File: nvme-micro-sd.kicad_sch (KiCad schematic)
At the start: 30 parts, among them J6 MicroSD_1140084168, J7 Bus_M.2_1-2199230-6, M2 Mech_M2_2280_H2.5mm

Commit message: [#53804] Clean SD&NVMe sch; Change NVMe to x4; Update 3V3 power sch
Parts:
- removed D14: SP3011-06UTG, antmicro-footprints:USON-14_3.5x1.35_P0.5mm, symbol antmicroTVSDiodes:SP3011-06UTG
- added D? (x2): PUSB3F96X_PASS, antmicro-footprints:Nexperia_DFN-10_2.5x1mm_P0.5mm, symbol antmicroTVSDiodes:PUSB3F96X_PASS
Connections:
- net GND: now also D?.3 (GND), D?.3 (GND), D?.8 (GND), D?.8 (GND)
- net SDIO.CLK: now also D?.5 (CH4), D?.6 (CH4)
- net SDIO.CMD: now also D?.1 (CH1), D?.10 (CH1)
- net SDIO.D0: now also D?.4 (CH3), D?.7 (CH3)
- net SDIO.D1: now also D?.2 (CH2), D?.9 (CH2)
- net SDIO.D2: now also D?.5 (CH4), D?.6 (CH4)
- net SDIO.D3: now also D?.4 (CH3), D?.7 (CH3)
- net at J6.9 (CD1), R81.2: now also D?.1 (CH1), D?.10 (CH1)
- net NVMe.TX3_N: now reaches J7.11 (PET3_N)
- net NVMe.TX3_P: now reaches J7.13 (PET3_P)
- net NVMe.RX2_N: now reaches J7.17 (PER2_N)
- net NVMe.RX2_P: now reaches J7.19 (PER2_P)
- net NVMe.TX2_N: now reaches J7.23 (PET2_N)
- net NVMe.TX2_P: now reaches J7.25 (PET2_P)
- net NVMe.RX1_N: now reaches J7.29 (PER1_N)
- net NVMe.RX1_P: now reaches J7.31 (PER1_P)
- net NVMe.TX1_N: now reaches J7.35 (PET1_N)
- net NVMe.TX1_P: now reaches J7.37 (PET1_P)
- net NVMe.RX3_N: now reaches J7.5 (PER3_N)
- net NVMe.RX3_P: now reaches J7.7 (PER3_P)
- net 3V3_RPi renamed +3V3
- net +3V3: now also D?.2 (CH2), D?.9 (CH2)
- net GPIO3 renamed SDIO.CD
- net NVMe.RX_N renamed NVMe.RX0_N
- net NVMe.RX_P renamed NVMe.RX0_P
- net NVMe.TX_N renamed NVMe.TX0_N
- net NVMe.TX_P renamed NVMe.TX0_P
- net PCIE_CLK_nREQ renamed NVMe.~{CLK_REQ}
- net PCIE_WAKE: no longer names the net of J7.54 (~{PEWAKE}), R89.2
- net PSCIE_nRST renamed NVMe.~{RST}
- no-connect marks 17 -> 4
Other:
- note added: "Micro SD card slot"
- note added: "Note: CM4 supports only PCIe 2.0x1"
- note removed: "Micro CD card slot"
- note removed: "TODO"
- moved on the sheet: C42, C43, C44, C45, C46, C47, C48, C49, C50, C51, C52, C53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

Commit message: [#53804] Visual cleanup for m.2/SD sch
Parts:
- removed C49, C50, C51: C_100n_0603, antmicro-footprints:C_0603_1608Metric, symbol antmicroCapacitors0603:C_100n_0603
- removed C52, C53, C54: C_1n_0603, antmicro-footprints:C_0603_1608Metric, symbol antmicroCapacitors0603:C_1n_0603
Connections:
- net +3V3: now also D?.5 (CH4), D?.6 (CH4); no longer D?.2 (CH2), D?.9 (CH2)
- net GND: now also SP9.1
- net SDIO.CD: now also D?.5 (CH4), D?.6 (CH4)
- net SDIO.CLK: now also D?.1 (CH1), D?.10 (CH1); no longer D?.5 (CH4), D?.6 (CH4)
- net SDIO.CMD: now also D?.4 (CH3), D?.7 (CH3); no longer D?.1 (CH1), D?.10 (CH1)
- net SDIO.D0: now also D?.2 (CH2), D?.9 (CH2); no longer D?.4 (CH3), D?.7 (CH3)
- net SDIO.D1: now also D?.4 (CH3), D?.7 (CH3); no longer D?.2 (CH2), D?.9 (CH2)
- net SDIO.D2: now also D?.1 (CH1), D?.10 (CH1); no longer D?.5 (CH4), D?.6 (CH4)
- net SDIO.D3: now also D?.2 (CH2), D?.9 (CH2); no longer D?.4 (CH3), D?.7 (CH3)
- net at J6.9 (CD1), R81.2: no longer D?.1 (CH1), D?.10 (CH1)
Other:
- note added: "Note: Place close to pins 12,14,16,18"
- note added: "Note: Place close to pins 2,4"
- note added: "Note: Place close to pins 70,72,74"
- note removed: "Capacitor cluster for pins 12,14,16,18"
- note removed: "Capacitor cluster for pins 2,4"
- note removed: "Capacitor cluster for pins 70,72,74"
- moved on the sheet: C42, C43, C44, C45, C46, C47, C48, D15, D?, J6, J7, M2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

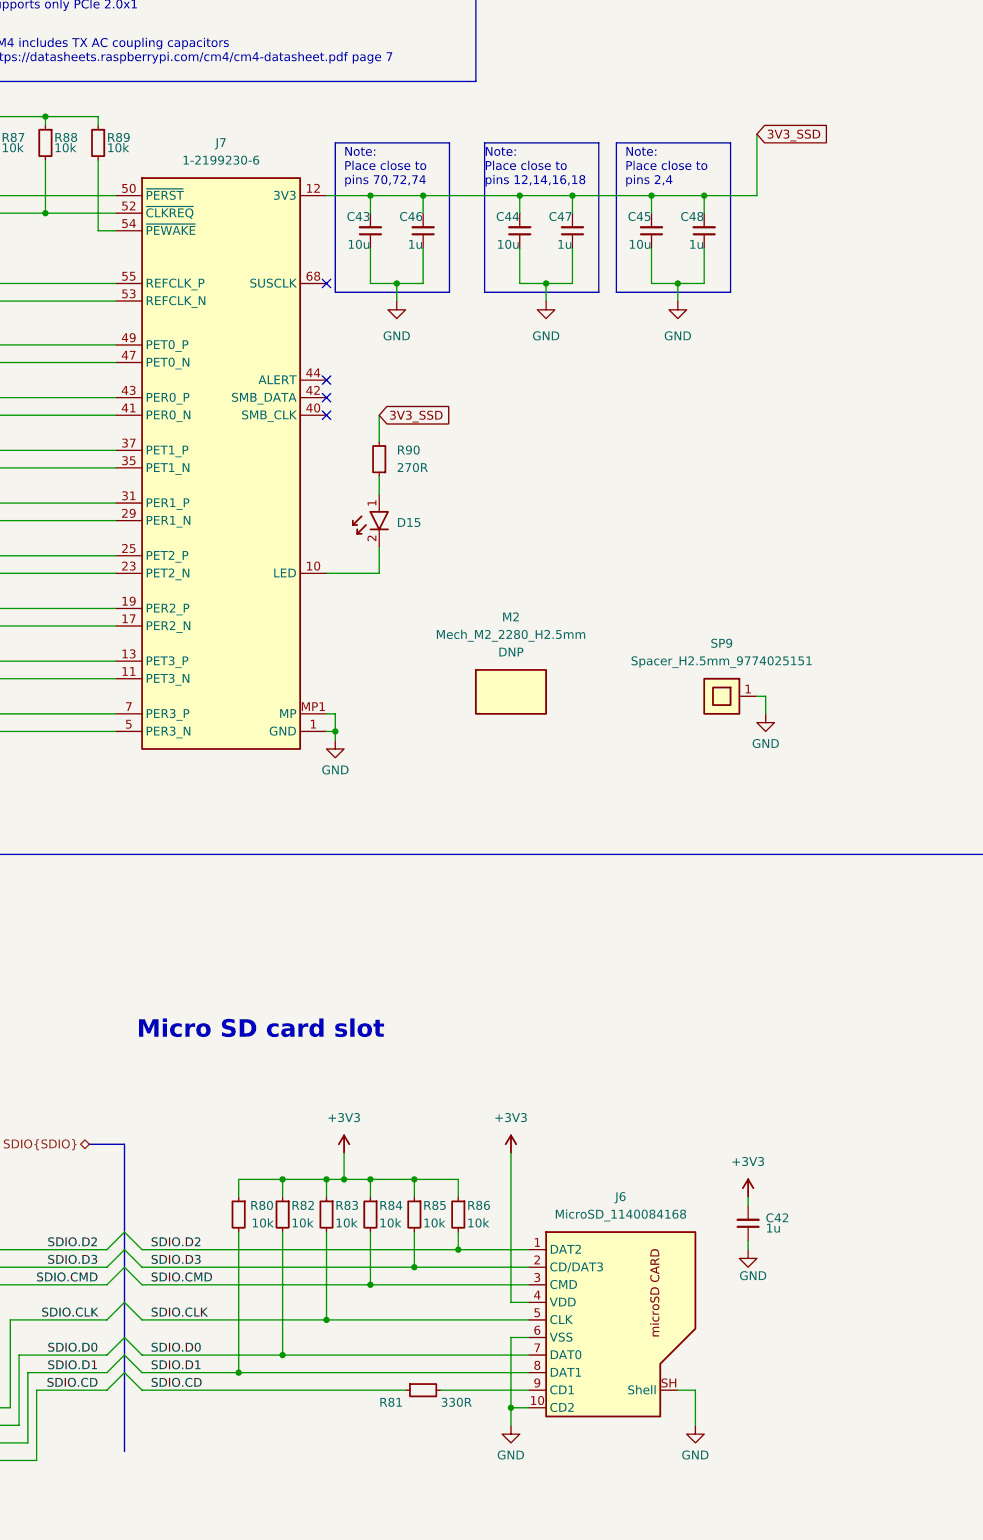
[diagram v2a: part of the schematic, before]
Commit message: [#54617] Apply changes pointed in review, related to nvme-micro-sd
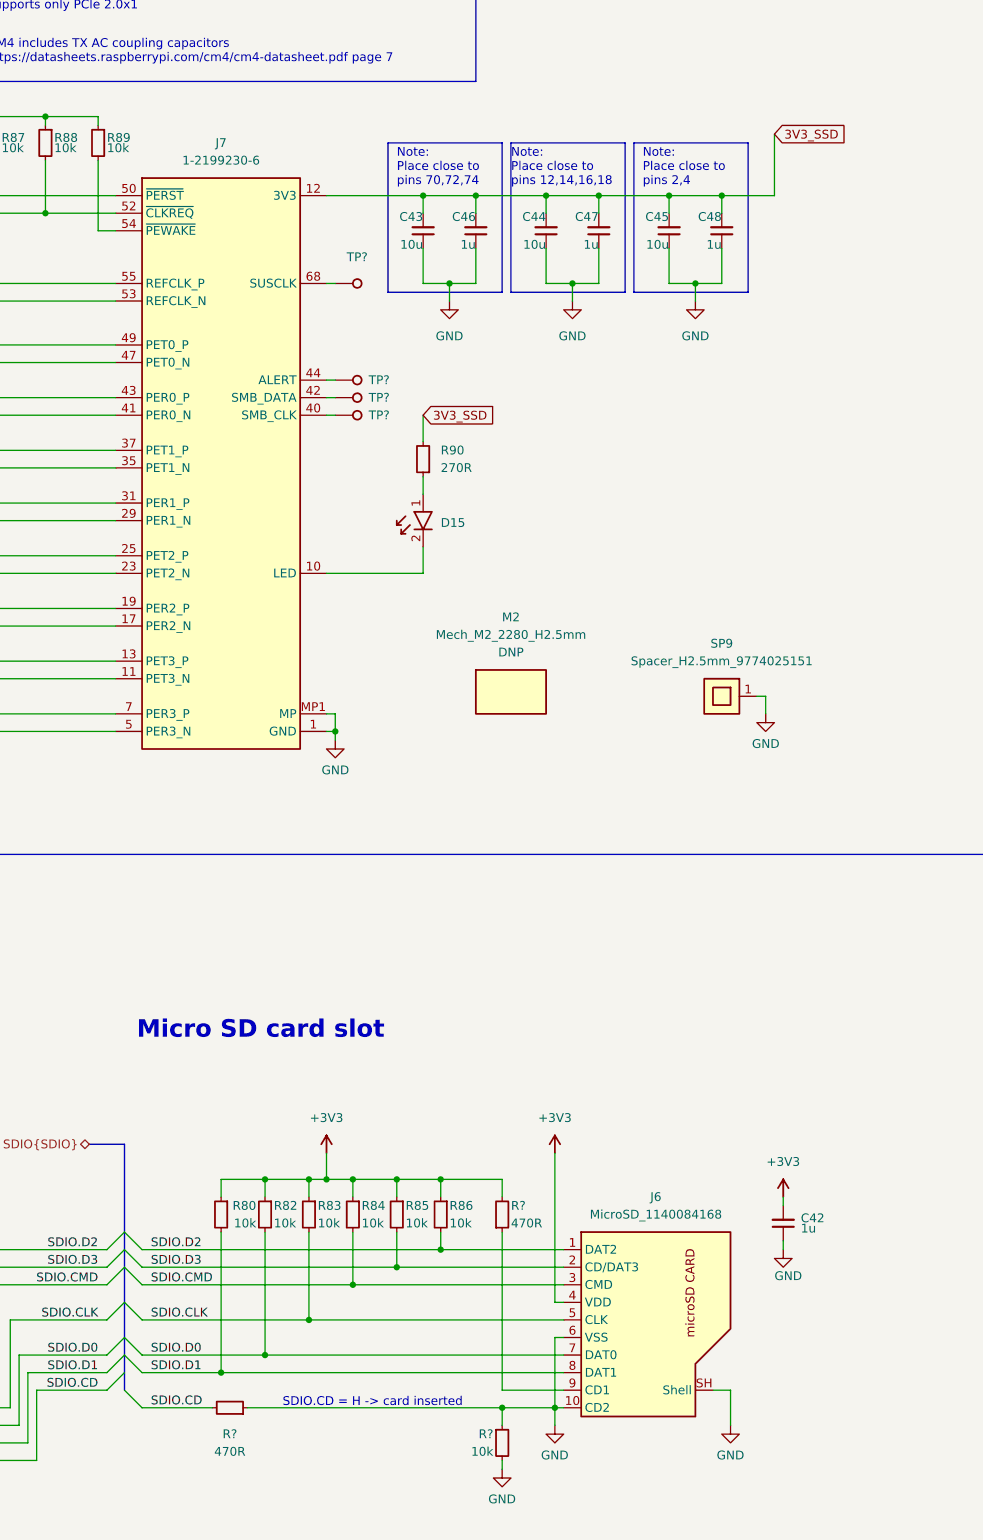
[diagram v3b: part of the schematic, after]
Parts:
- removed R81: R_330R_0402, antmicro-footprints:R_0402_1005Metric, symbol antmicroResistors0402:R_330R_0402
- added R? (x2): R_470R_0402, antmicro-footprints:R_0402_1005Metric, symbol antmicroResistors0402:R_470R_0402
- added R?: R_10k_0402, antmicro-footprints:R_0402_1005Metric, symbol antmicroResistors0402:R_10k_0402
- added TP? (x4): TP_0.75mm_SMD, antmicro-footprints:TP_SMD_0.75mm, symbol antmicroTestPoints:TP_0.75mm_SMD
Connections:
- net +3V3: now also R?.2
- net GND: now also R?.1, R?.1, R?.2
- net SDIO.CD: now also R?.2
- net at J6.9 (CD1): now also R?.1
- net at J7.40 (SMB_CLK): now also TP?.1
- net at J7.42 (SMB_DATA): now also TP?.1
- net at J7.44 (ALERT): now also TP?.1
- net at J7.68 (SUSCLK): now also TP?.1
- no-connect marks 4 -> 0
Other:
- note added: "SDIO.CD = H -> card inserted"
- moved on the sheet: C42, C43, C44, C45, C46, C47, C48, D15, J6, R80, R82, R83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

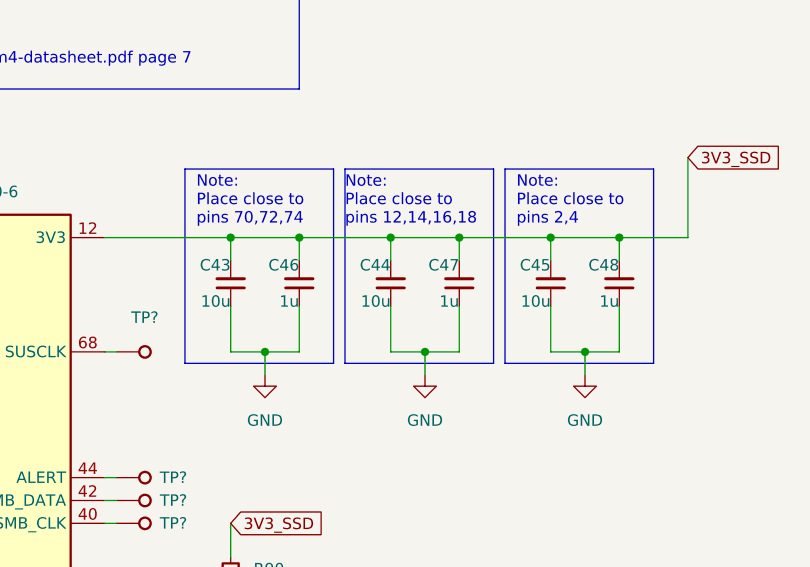
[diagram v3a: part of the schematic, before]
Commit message: [#54617] Reduce capacitors diversity
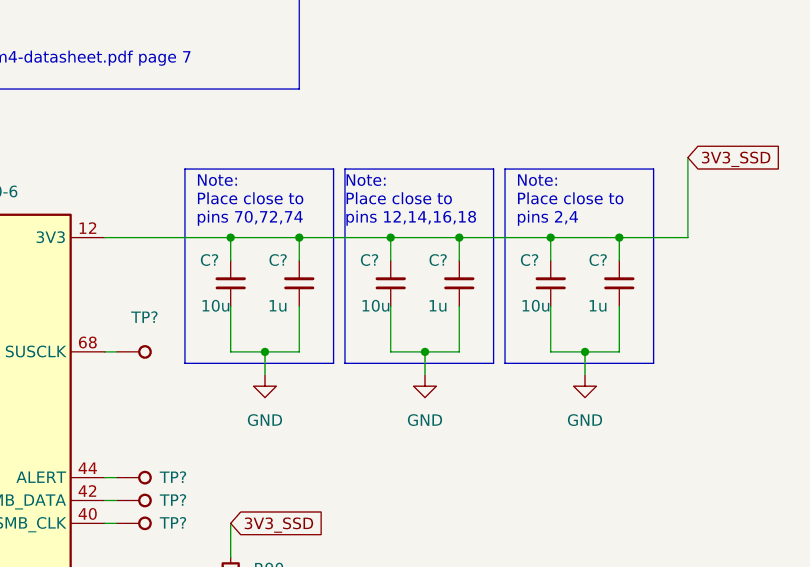
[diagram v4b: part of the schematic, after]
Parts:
- removed C43, C44, C45: C_10u_0603, antmicro-footprints:C_0603_1608Metric, symbol antmicroCapacitors0603:C_10u_0603
- removed C46, C47, C48: C_1u_0603, antmicro-footprints:C_0603_1608Metric, symbol antmicroCapacitors0603:C_1u_0603
- added C? (x3): C_1u_0402, antmicro-footprints:C_0402_1005Metric, symbol antmicroCapacitors0402:C_1u_0402
- added C? (x3): C_10u_0402, antmicro-footprints:C_0402_1005Metric, symbol antmicroCapacitors0402:C_10u_0402
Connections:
- net 3V3_SSD: now also C?.2, C?.2, C?.2, C?.2, C?.2, C?.2
- net GND: now also C?.1, C?.1, C?.1, C?.1, C?.1, C?.1

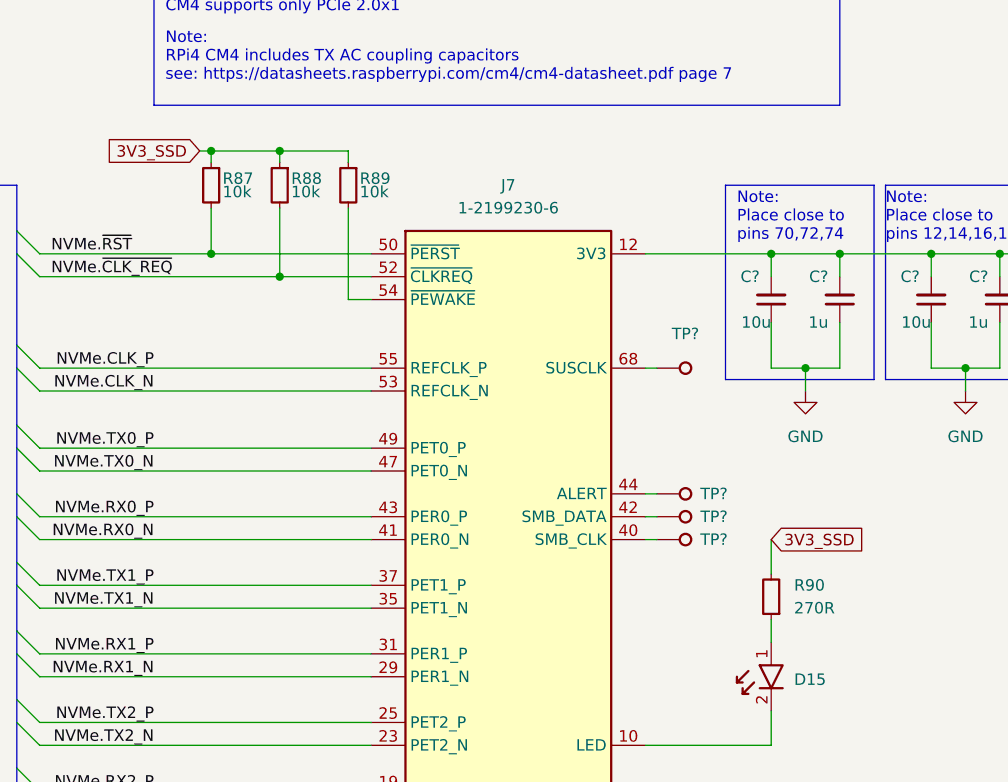
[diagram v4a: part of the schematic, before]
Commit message: [#54617] Reduce resistors diversity (switch size to 0402)
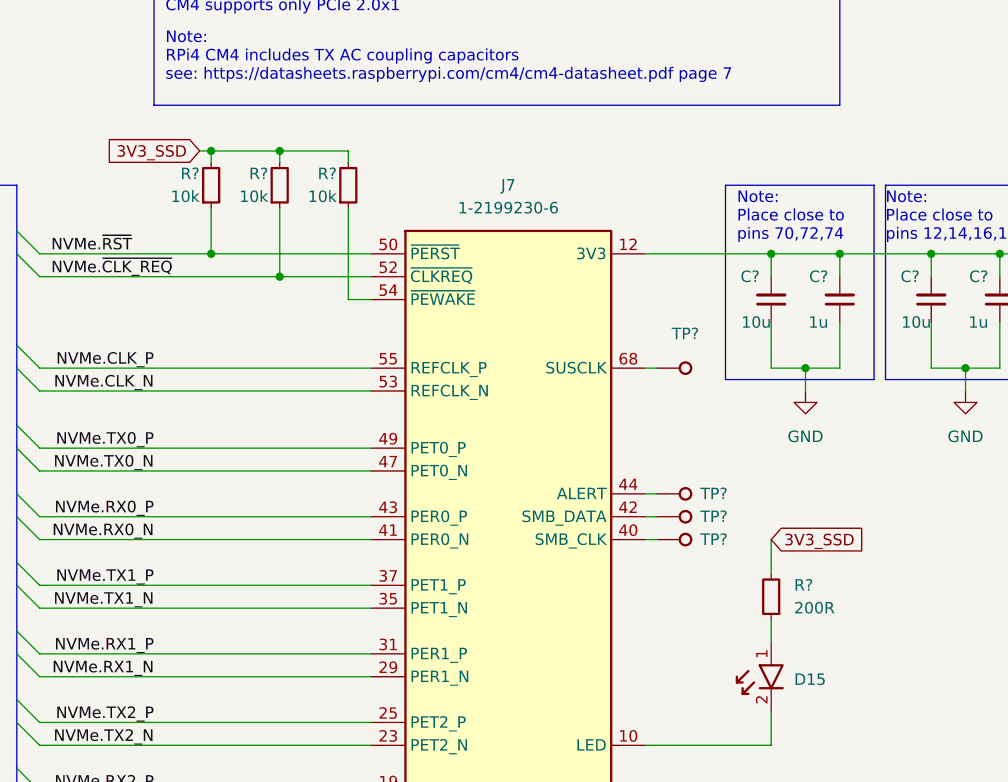
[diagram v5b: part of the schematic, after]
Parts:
- removed R87, R88, R89: R_10k_0603, antmicro-footprints:R_0603_1608Metric, symbol antmicroResistors0603:R_10k_0603
- removed R90: R_270R_0603, antmicro-footprints:R_0603_1608Metric, symbol antmicroResistors0603:R_270R_0603
- added R?: R_200R_0402, antmicro-footprints:R_0402_1005Metric, symbol antmicroResistors0402:R_200R_0402
- added R? (x3): R_10k_0402, antmicro-footprints:R_0402_1005Metric, symbol antmicroResistors0402:R_10k_0402
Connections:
- net 3V3_SSD: now also R?.2, R?.2, R?.2, R?.2
- net NVMe.~{CLK_REQ}: now also R?.1
- net NVMe.~{RST}: now also R?.1
- net at J7.54 (~{PEWAKE}): now also R?.1
- net at D15.1: now also R?.1
